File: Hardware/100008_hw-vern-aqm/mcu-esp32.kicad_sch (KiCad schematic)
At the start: 32 parts, among them Q1 BC817, Q2 BC817, SW1 SW_Push, SW2 SW_Push, U2 ESP32-S3-WROOM-1, U3 CP2102N-Axx-xQFN24

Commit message: pcb layout
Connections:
- net LCD_BACKLIGHT: now also U2.11 (GPIO18/U1RXD/ADC2_CH7/CLK_OUT3); no longer U2.19 (GPIO11/TOUCH11/ADC2_CH0/FSPID/FSPIIO5/SUBSPID)
- net LCD_DC/RS: now also U2.12 (GPIO8/TOUCH8/ADC1_CH7/SUBSPICS1); no longer U2.18 (GPIO10/TOUCH10/ADC1_CH9/FSPICS0/FSPIIO4/SUBSPICS0)
- net SD_CS(D3): now also U2.19 (GPIO11/TOUCH11/ADC2_CH0/FSPID/FSPIIO5/SUBSPID); no longer U2.20 (GPIO12/TOUCH12/ADC2_CH1/FSPICLK/FSPIIO6/SUBSPICLK)
- net SD_MISO(D0): now also U2.21 (GPIO13/TOUCH13/ADC2_CH2/FSPIQ/FSPIIO7/SUBSPIQ); no longer U2.22 (GPIO14/TOUCH14/ADC2_CH3/FSPIWP/FSPIDQS/SUBSPIWP)
- net SD_MOSI(CMD): now also U2.20 (GPIO12/TOUCH12/ADC2_CH1/FSPICLK/FSPIIO6/SUBSPICLK); no longer U2.21 (GPIO13/TOUCH13/ADC2_CH2/FSPIQ/FSPIIO7/SUBSPIQ)
- net SD_SCK(CLK): now also U2.22 (GPIO14/TOUCH14/ADC2_CH3/FSPIWP/FSPIDQS/SUBSPIWP); no longer U2.10 (GPIO17/U1TXD/ADC2_CH6)
- net SPI_MISO: now also U2.5 (GPIO5/TOUCH5/ADC1_CH4); no longer U2.6 (GPIO6/TOUCH6/ADC1_CH5)
- net SPI_MOSI: now also U2.6 (GPIO6/TOUCH6/ADC1_CH5); no longer U2.7 (GPIO7/TOUCH7/ADC1_CH6)
- net SPI_SCK: now also U2.10 (GPIO17/U1TXD/ADC2_CH6); no longer U2.12 (GPIO8/TOUCH8/ADC1_CH7/SUBSPICS1)
- net SPI_nCS_LCD: now also U2.18 (GPIO10/TOUCH10/ADC1_CH9/FSPICS0/FSPIIO4/SUBSPICS0); no longer U2.4 (GPIO4/TOUCH4/ADC1_CH3)
- net SPI_nCS_TOUCH: now also U2.7 (GPIO7/TOUCH7/ADC1_CH6); no longer U2.5 (GPIO5/TOUCH5/ADC1_CH4)

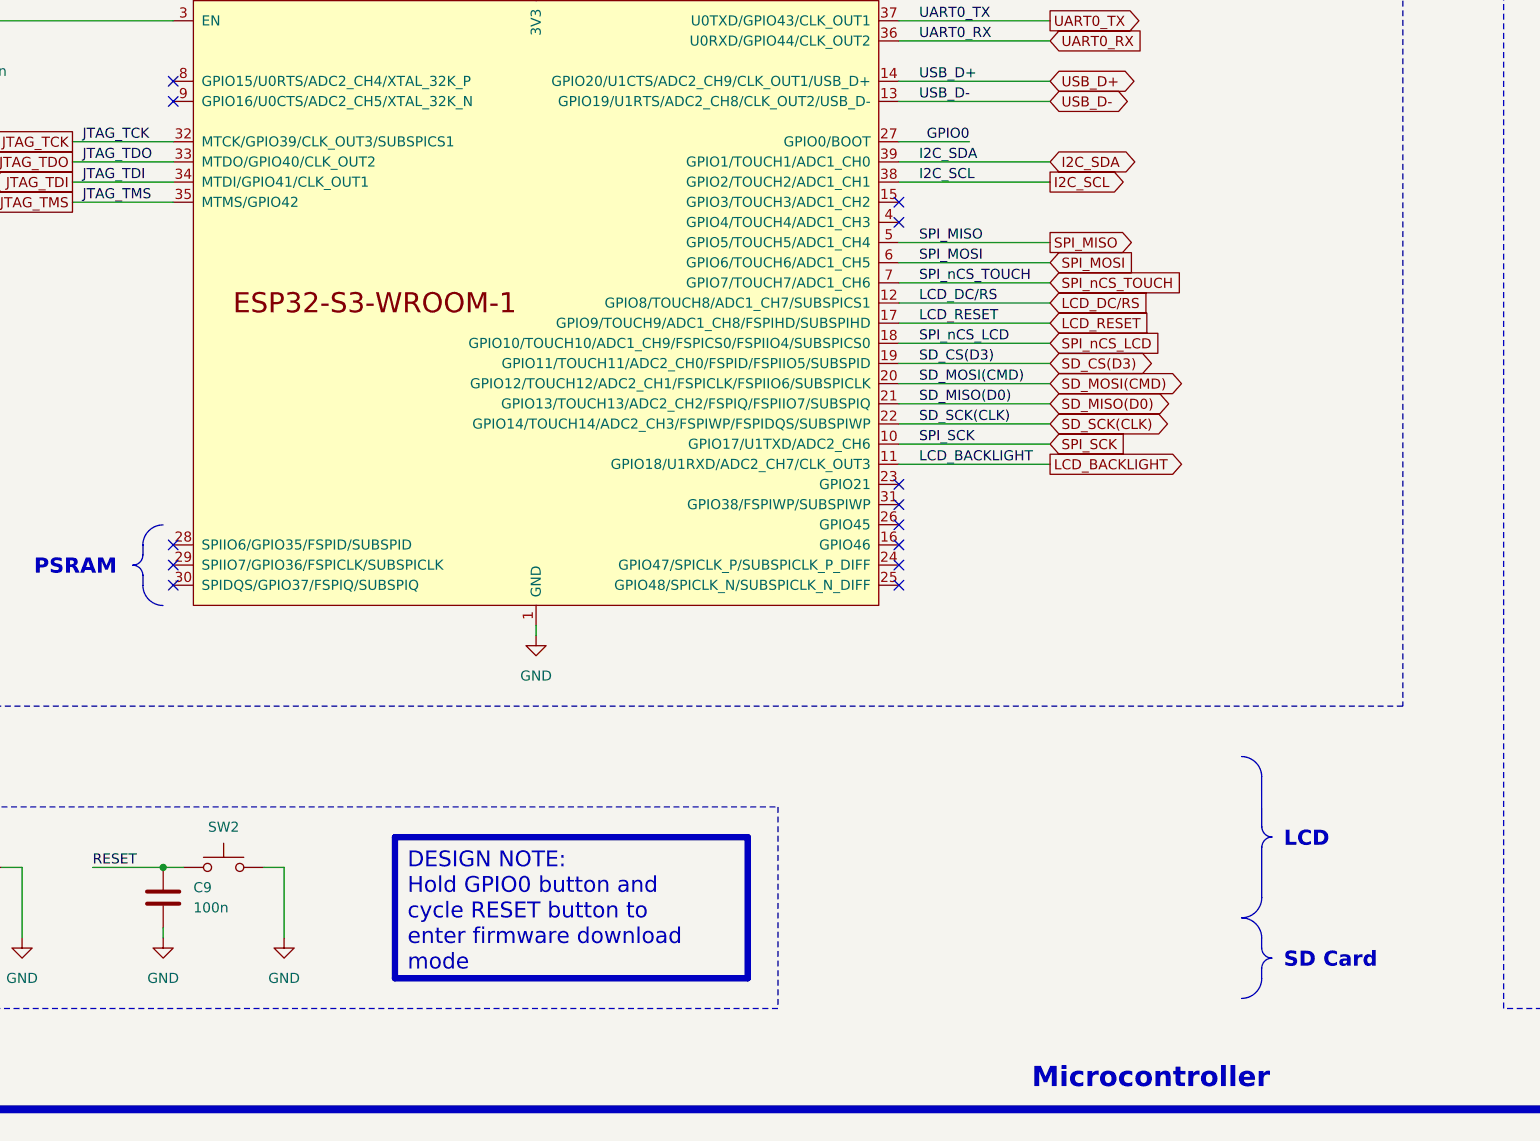
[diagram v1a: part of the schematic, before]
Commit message: PCB routing and DRC fixes
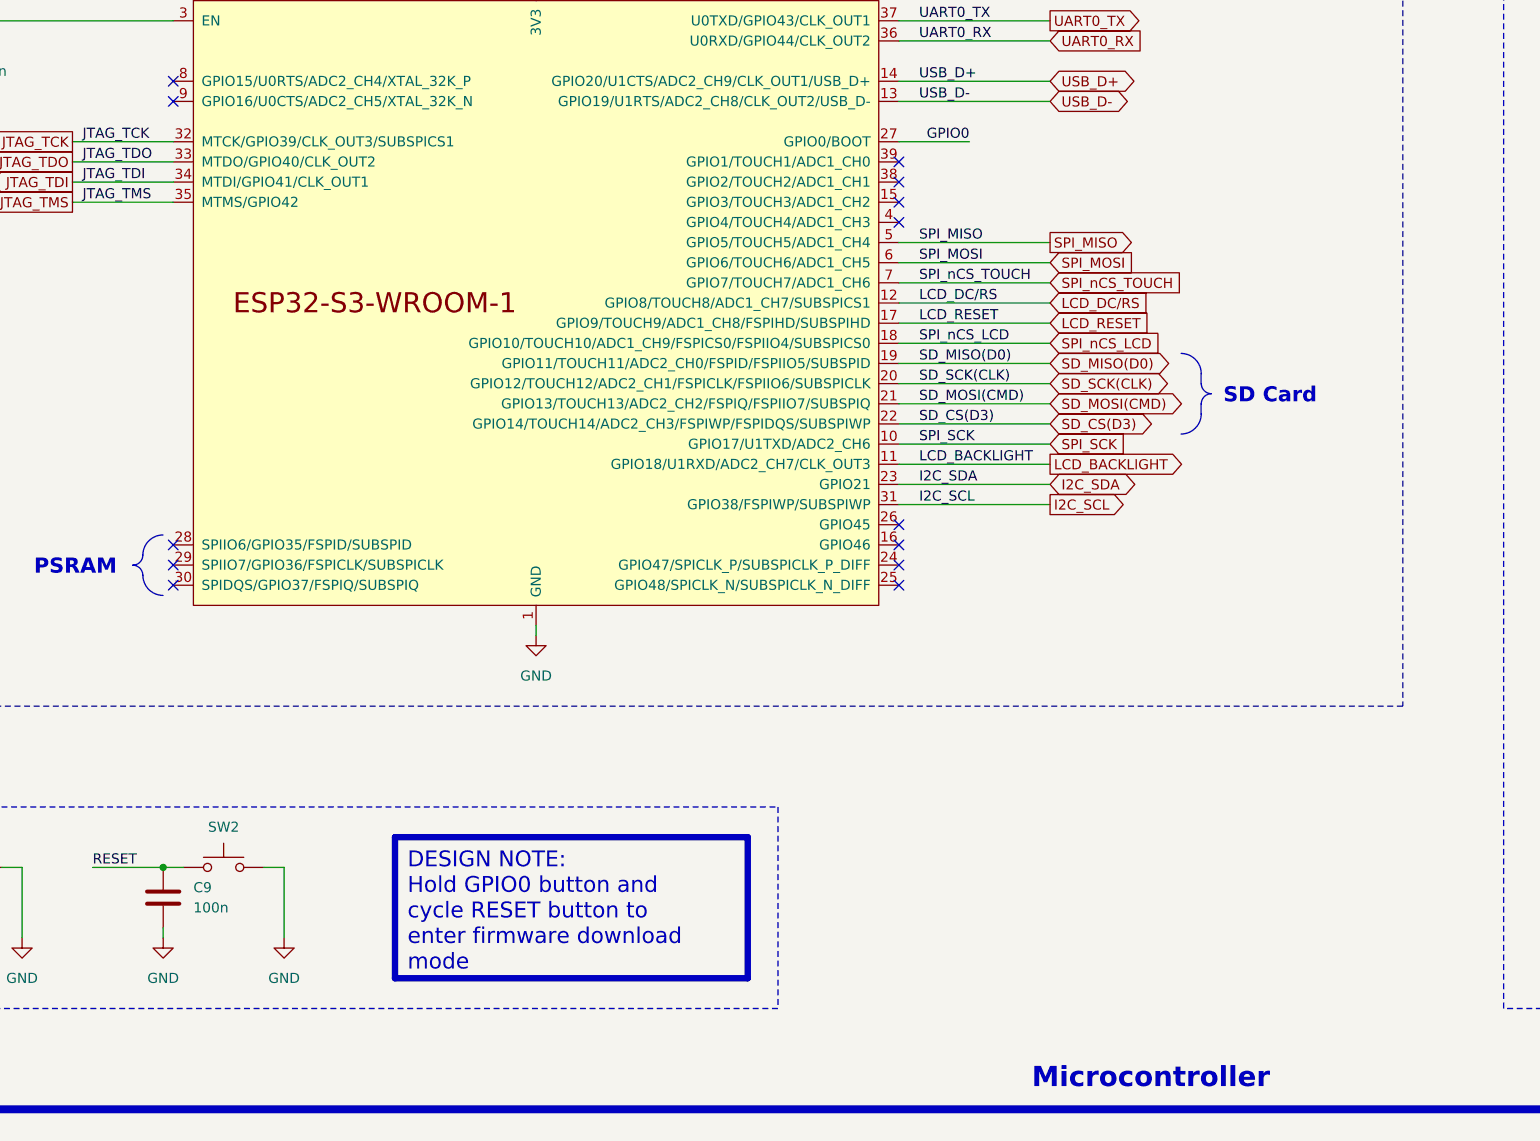
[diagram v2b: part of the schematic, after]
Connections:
- net I2C_SCL: now also U2.31 (GPIO38/FSPIWP/SUBSPIWP); no longer U2.38 (GPIO2/TOUCH2/ADC1_CH1)
- net I2C_SDA: now also U2.23 (GPIO21); no longer U2.39 (GPIO1/TOUCH1/ADC1_CH0)
- net SD_CS(D3): now also U2.22 (GPIO14/TOUCH14/ADC2_CH3/FSPIWP/FSPIDQS/SUBSPIWP); no longer U2.19 (GPIO11/TOUCH11/ADC2_CH0/FSPID/FSPIIO5/SUBSPID)
- net SD_MISO(D0): now also U2.19 (GPIO11/TOUCH11/ADC2_CH0/FSPID/FSPIIO5/SUBSPID); no longer U2.21 (GPIO13/TOUCH13/ADC2_CH2/FSPIQ/FSPIIO7/SUBSPIQ)
- net SD_MOSI(CMD): now also U2.21 (GPIO13/TOUCH13/ADC2_CH2/FSPIQ/FSPIIO7/SUBSPIQ); no longer U2.20 (GPIO12/TOUCH12/ADC2_CH1/FSPICLK/FSPIIO6/SUBSPICLK)
- net SD_SCK(CLK): now also U2.20 (GPIO12/TOUCH12/ADC2_CH1/FSPICLK/FSPIIO6/SUBSPICLK); no longer U2.22 (GPIO14/TOUCH14/ADC2_CH3/FSPIWP/FSPIDQS/SUBSPIWP)

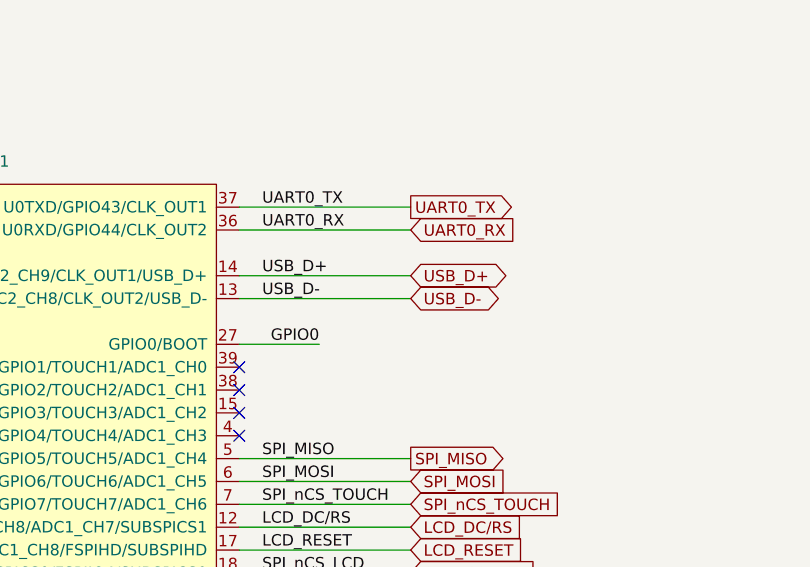
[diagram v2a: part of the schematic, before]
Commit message: fixing DRC issues
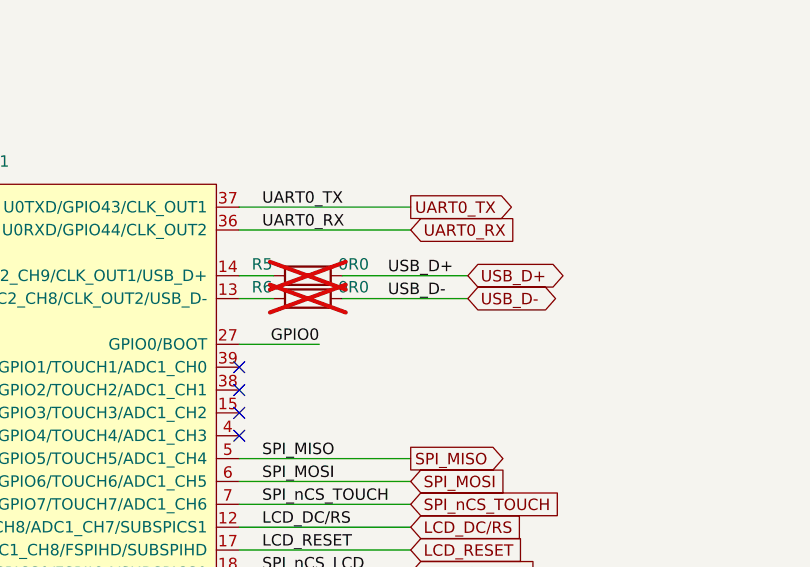
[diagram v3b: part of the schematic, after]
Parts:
- added R5, R6: 0R0, Resistor_SMD:R_0603_1608Metric, symbol Device:R
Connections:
- net USB_D+: now also R5.1; no longer U2.14 (GPIO20/U1CTS/ADC2_CH9/CLK_OUT1/USB_D+)
- net USB_D-: now also R6.1; no longer U2.13 (GPIO19/U1RTS/ADC2_CH8/CLK_OUT2/USB_D-)
- new net: R6.2, U2.13 (GPIO19/U1RTS/ADC2_CH8/CLK_OUT2/USB_D-)
- new net: R5.2, U2.14 (GPIO20/U1CTS/ADC2_CH9/CLK_OUT1/USB_D+)
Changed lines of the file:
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@@
 	(wire
 		(pts
+			(xy 189.23 86.36) (xy 203.2 86.36)
+		)
+		(stroke
+			(width 0)
+			(type default)
+		)
+	)
+	(wire
+		(pts
 			(xy 335.28 185.42) (xy 337.82 185.42)
 		)
@@
 	(wire
 		(pts
-			(xy 177.8 88.9) (xy 196.85 88.9)
-		)
-		(stroke
-			(width 0)
-			(type default)
-		)
-	)
-	(wire
-		(pts
 			(xy 370.84 109.22) (xy 370.84 110.49)
 		)
@@
 	(wire
 		(pts
-			(xy 177.8 86.36) (xy 196.85 86.36)
-		)
-		(stroke
-			(width 0)
-			(type default)
-		)
-	)
-	(wire
-		(pts
 			(xy 177.8 114.3) (xy 196.85 114.3)
 		)
@@
 	(wire
 		(pts
+			(xy 181.61 86.36) (xy 177.8 86.36)
+		)
+		(stroke
+			(width 0)
+			(type default)
+		)
+	)
+	(wire
+		(pts
 			(xy 345.44 175.26) (xy 345.44 176.53)
 		)
@@
 	(wire
 		(pts
+			(xy 189.23 88.9) (xy 203.2 88.9)
+		)
+		(stroke
+			(width 0)
+			(type default)
+		)
+	)
+	(wire
+		(pts
 			(xy 335.28 93.98) (xy 363.22 93.98)
 		)
@@
 	(wire
 		(pts
+			(xy 181.61 88.9) (xy 177.8 88.9)
+		)
+		(stroke
+			(width 0)
+			(type default)
+		)
+	)
+	(wire
+		(pts
 			(xy 284.48 88.9) (xy 284.48 74.93)
 		)
@@
 		)
 	)
-	(label "USB_D-"
-		(at 180.34 88.9 0)
-		(fields_autoplaced yes)
-		(effects
-			(font
-				(size 1.27 1.27)
-			)
-			(justify left bottom)
-		)
-	)
 	(label "GPIO0"
 		(at 368.3 190.5 180)
@@
 		)
 	)
-	(label "USB_D+"
-		(at 180.34 86.36 0)
+	(label "SD_SCK(CLK)"
+		(at 180.34 124.46 0)
 		(fields_autoplaced yes)
 		(effects
@@
 		)
 	)
-	(label "SD_SCK(CLK)"
-		(at 180.34 124.46 0)
+	(label "USB_D+"
+		(at 194.31 86.36 0)
 		(fields_autoplaced yes)
 		(effects
@@
 		)
 	)
+	(label "USB_D-"
+		(at 194.31 88.9 0)
+		(fields_autoplaced yes)
+		(effects
+			(font
+				(size 1.27 1.27)
+			)
+			(justify left bottom)
+		)
+	)
 	(label "UART0_nDTR"
 		(at 364.49 101.6 180)
@@
 		)
 	)
-	(global_label "USB_D+"
-		(shape bidirectional)
-		(at 196.85 86.36 0)
-		(fields_autoplaced yes)
-		(effects
-			(font
-				(size 1.27 1.27)
-			)
-			(justify left)
-		)
-		(property "Intersheetrefs" "${INTERSHEET_REFS}"
-			(at 207.4552 86.36 0)
-			(effects
-				(font
-					(size 1.27 1.27)
-				)
-				(justify left)
-				(hide yes)
-			)
-		)
-	)
 	(global_label "USB_D-"
 		(shape bidirectional)
@@
 		)
 	)
-	(global_label "USB_D-"
+	(global_label "USB_D+"
 		(shape bidirectional)
-		(at 196.85 88.9 0)
+		(at 203.2 86.36 0)
 		(fields_autoplaced yes)
 		(effects
@@
 		)
 		(property "Intersheetrefs" "${INTERSHEET_REFS}"
-			(at 208.5665 88.9 0)
+			(at 213.8052 86.36 0)
 			(effects
 				(font
@@
 		)
 	)
+	(global_label "USB_D-"
+		(shape bidirectional)
+		(at 203.2 88.9 0)
+		(fields_autoplaced yes)
+		(effects
+			(font
+				(size 1.27 1.27)
+			)
+			(justify left)
+		)
+		(property "Intersheetrefs" "${INTERSHEET_REFS}"
+			(at 214.9165 88.9 0)
+			(effects
+				(font
+					(size 1.27 1.27)
+				)
+				(justify left)
+				(hide yes)
+			)
+		)
+	)
 	(global_label "JTAG_TMS"
 		(shape output)
@@
 	)
 	(symbol
+		(lib_id "Device:R")
+		(at 185.42 88.9 270)
+		(mirror x)
+		(unit 1)
+		(exclude_from_sim no)
+		(in_bom yes)
+		(on_board yes)
+		(dnp yes)
+		(property "Reference" "R6"
+			(at 180.34 87.63 90)
+			(effects
+				(font
+					(size 1.27 1.27)
+				)
+			)
+		)
+		(property "Value" "0R0"
+			(at 190.5 87.63 90)
+			(effects
+				(font
+					(size 1.27 1.27)
+				)
+			)
+		)
+		(property "Footprint" "Resistor_SMD:R_0603_1608Metric"
+			(at 185.42 90.678 90)
+			(effects
+				(font
+					(size 1.27 1.27)
+				)
+				(hide yes)
+			)
+		)
+		(property "Datasheet" "~"
+			(at 185.42 88.9 0)
+			(effects
+				(font
+					(size 1.27 1.27)
+				)
+				(hide yes)
+			)
+		)
+		(property "Description" "Resistor"
+			(at 185.42 88.9 0)
+			(effects
+				(font
+					(size 1.27 1.27)
+				)
+				(hide yes)
+			)
+		)
+		(pin "1"
+		)
+		(pin "2"
+		)
+		(instances
+			(project "100008_hw-vern-aqm"
+				(path "/0650c7a8-acba-429c-9f8e-eec0baf0bc1c/fede4c36-00cc-4d3d-b71c-5243ba232202/e6015f1e-cbce-46f4-85e1-3d5463a17dc1"
+					(reference "R6")
+					(unit 1)
+				)
+			)
+		)
+	)
+	(symbol
 		(lib_id "Transistor_BJT:BC817")
 		(at 342.9 185.42 0)
@@
 					(unit 1)
 				)
+			)
+		)
+	)
+	(symbol
+		(lib_id "Device:R")
+		(at 185.42 86.36 270)
+		(mirror x)
+		(unit 1)
+		(exclude_from_sim no)
+		(in_bom yes)
+		(on_board yes)
+		(dnp yes)
+		(property "Reference" "R5"
+			(at 180.34 85.09 90)
+			(effects
+				(font
+					(size 1.27 1.27)
+				)
+			)
+		)
+		(property "Value" "0R0"
+			(at 190.5 85.09 90)
+			(effects
+				(font
+					(size 1.27 1.27)
+				)
+			)
+		)
+		(property "Footprint" "Resistor_SMD:R_0603_1608Metric"
+			(at 185.42 88.138 90)
+			(effects
+				(font
+					(size 1.27 1.27)
+				)
+				(hide yes)
+			)
+		)
+		(property "Datasheet" "~"
+			(at 185.42 86.36 0)
+			(effects
+				(font
+					(size 1.27 1.27)
+				)
+				(hide yes)
+			)
+		)
+		(property "Description" "Resistor"
+			(at 185.42 86.36 0)
+			(effects
+				(font
+					(size 1.27 1.27)
+				)
+				(hide yes)
+			)
+		)
+		(pin "1"
+		)
+		(pin "2"
+		)
+		(instances
+			(project "100008_hw-vern-aqm"
+				(path "/0650c7a8-acba-429c-9f8e-eec0baf0bc1c/fede4c36-00cc-4d3d-b71c-5243ba232202/e6015f1e-cbce-46f4-85e1-3d5463a17dc1"
+					(reference "R5")
+					(unit 1)
+				)

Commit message: schematic release, pcb release
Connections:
- net D-: now reaches R6.2, U2.13 (GPIO19/U1RTS/ADC2_CH8/CLK_OUT2/USB_D-)
- net D+: now reaches R5.2, U2.14 (GPIO20/U1CTS/ADC2_CH9/CLK_OUT1/USB_D+)
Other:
- note added: "ESP32-S3 Datasheet"
- note added: "ESP32-S3 Technical Reference Manual"
- note removed: "Flexible I/O source configuration"
- note removed: "Flexible I/O worked examples"
- moved on the sheet: R5, R6
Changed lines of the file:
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@@
 	(wire
 		(pts
-			(xy 189.23 86.36) (xy 203.2 86.36)
+			(xy 195.58 86.36) (xy 209.55 86.36)
 		)
 		(stroke
@@
 	(wire
 		(pts
-			(xy 181.61 86.36) (xy 177.8 86.36)
+			(xy 187.96 86.36) (xy 177.8 86.36)
 		)
 		(stroke
@@
 	(wire
 		(pts
-			(xy 189.23 88.9) (xy 203.2 88.9)
+			(xy 195.58 88.9) (xy 209.55 88.9)
 		)
 		(stroke
@@
 	(wire
 		(pts
-			(xy 181.61 88.9) (xy 177.8 88.9)
+			(xy 187.96 88.9) (xy 177.8 88.9)
 		)
 		(stroke
@@
 		)
 	)
-	(text "Flexible I/O worked examples"
+	(text "ESP32-S3 Datasheet"
 		(exclude_from_sim no)
 		(at 265.43 254 0)
@@
 			)
 			(justify left bottom)
-			(href "https://jpieper.com/2022/06/30/flexible-i-o-worked-examples/")
+			(href "https://www.espressif.com/sites/default/files/documentation/esp32-s3_datasheet_en.pdf")
 		)
 	)
@@
 		)
 	)
-	(text "Flexible I/O source configuration"
+	(text "ESP32-S3 Technical Reference Manual"
 		(exclude_from_sim no)
 		(at 265.43 256.54 0)
@@
 			)
 			(justify left bottom)
-			(href "https://jpieper.com/2022/06/28/flexible-i-o-source-configuration/")
+			(href "https://www.espressif.com/sites/default/files/documentation/esp32-s3_technical_reference_manual_en.pdf#spi")
 		)
 	)
@@
 	)
 	(label "USB_D+"
-		(at 194.31 86.36 0)
+		(at 200.66 86.36 0)
 		(fields_autoplaced yes)
 		(effects
@@
 		)
 	)
+	(label "D-"
+		(at 180.34 88.9 0)
+		(fields_autoplaced yes)
+		(effects
+			(font
+				(size 1.27 1.27)
+			)
+			(justify left bottom)
+		)
+	)
+	(label "D+"
+		(at 180.34 86.36 0)
+		(fields_autoplaced yes)
+		(effects
+			(font
+				(size 1.27 1.27)
+			)
+			(justify left bottom)
+		)
+	)
 	(label "SD_MOSI(CMD)"
 		(at 180.34 127 0)
@@
 	)
 	(label "USB_D-"
-		(at 194.31 88.9 0)
+		(at 200.66 88.9 0)
 		(fields_autoplaced yes)
 		(effects
@@
 	(global_label "USB_D+"
 		(shape bidirectional)
-		(at 203.2 86.36 0)
+		(at 209.55 86.36 0)
 		(fields_autoplaced yes)
 		(effects
@@
 		)
 		(property "Intersheetrefs" "${INTERSHEET_REFS}"
-			(at 213.8052 86.36 0)
+			(at 220.1552 86.36 0)
 			(effects
 				(font
@@
 	(global_label "USB_D-"
 		(shape bidirectional)
-		(at 203.2 88.9 0)
+		(at 209.55 88.9 0)
 		(fields_autoplaced yes)
 		(effects
@@
 		)
 		(property "Intersheetrefs" "${INTERSHEET_REFS}"
-			(at 214.9165 88.9 0)
+			(at 221.2665 88.9 0)
 			(effects
 				(font
@@
 	(symbol
 		(lib_id "Device:R")
-		(at 185.42 88.9 270)
+		(at 191.77 88.9 270)
 		(mirror x)
 		(unit 1)
@@
 		(dnp yes)
 		(property "Reference" "R6"
-			(at 180.34 87.63 90)
+			(at 186.69 87.63 90)
 			(effects
 				(font
@@
 		)
 		(property "Value" "0R0"
-			(at 190.5 87.63 90)
+			(at 196.85 87.63 90)
 			(effects
 				(font
@@
 		)
 		(property "Footprint" "Resistor_SMD:R_0603_1608Metric"
-			(at 185.42 90.678 90)
+			(at 191.77 90.678 90)
 			(effects
 				(font
@@
 		)
 		(property "Datasheet" "~"
-			(at 185.42 88.9 0)
+			(at 191.77 88.9 0)
 			(effects
 				(font
@@
 		)
 		(property "Description" "Resistor"
-			(at 185.42 88.9 0)
+			(at 191.77 88.9 0)
 			(effects
 				(font
@@
 	(symbol
 		(lib_id "Device:R")
-		(at 185.42 86.36 270)
+		(at 191.77 86.36 270)
 		(mirror x)
 		(unit 1)
@@
 		(dnp yes)
 		(property "Reference" "R5"
-			(at 180.34 85.09 90)
+			(at 186.69 85.09 90)
 			(effects
 				(font
@@
 		)
 		(property "Value" "0R0"
-			(at 190.5 85.09 90)
+			(at 196.85 85.09 90)
 			(effects
 				(font
@@
 		)
 		(property "Footprint" "Resistor_SMD:R_0603_1608Metric"
-			(at 185.42 88.138 90)
+			(at 191.77 88.138 90)
 			(effects
 				(font
@@
 		)
 		(property "Datasheet" "~"
-			(at 185.42 86.36 0)
+			(at 191.77 86.36 0)
 			(effects
 				(font
@@
 		)
 		(property "Description" "Resistor"
-			(at 185.42 86.36 0)
+			(at 191.77 86.36 0)
 			(effects
 				(font
